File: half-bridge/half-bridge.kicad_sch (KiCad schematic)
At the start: 121 parts, among them J1 Conn_01x11_Pin, J2 MountingHole_Pad, J3 Conn_01x11_Pin, J4 Conn_01x11_Pin, J5 Conn_01x11_Pin, J6 Conn_01x11_Pin, J7 MountingHole_Pad, J8 MountingHole_Pad, J9 MountingHole_Pad, Q1 EPC2306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

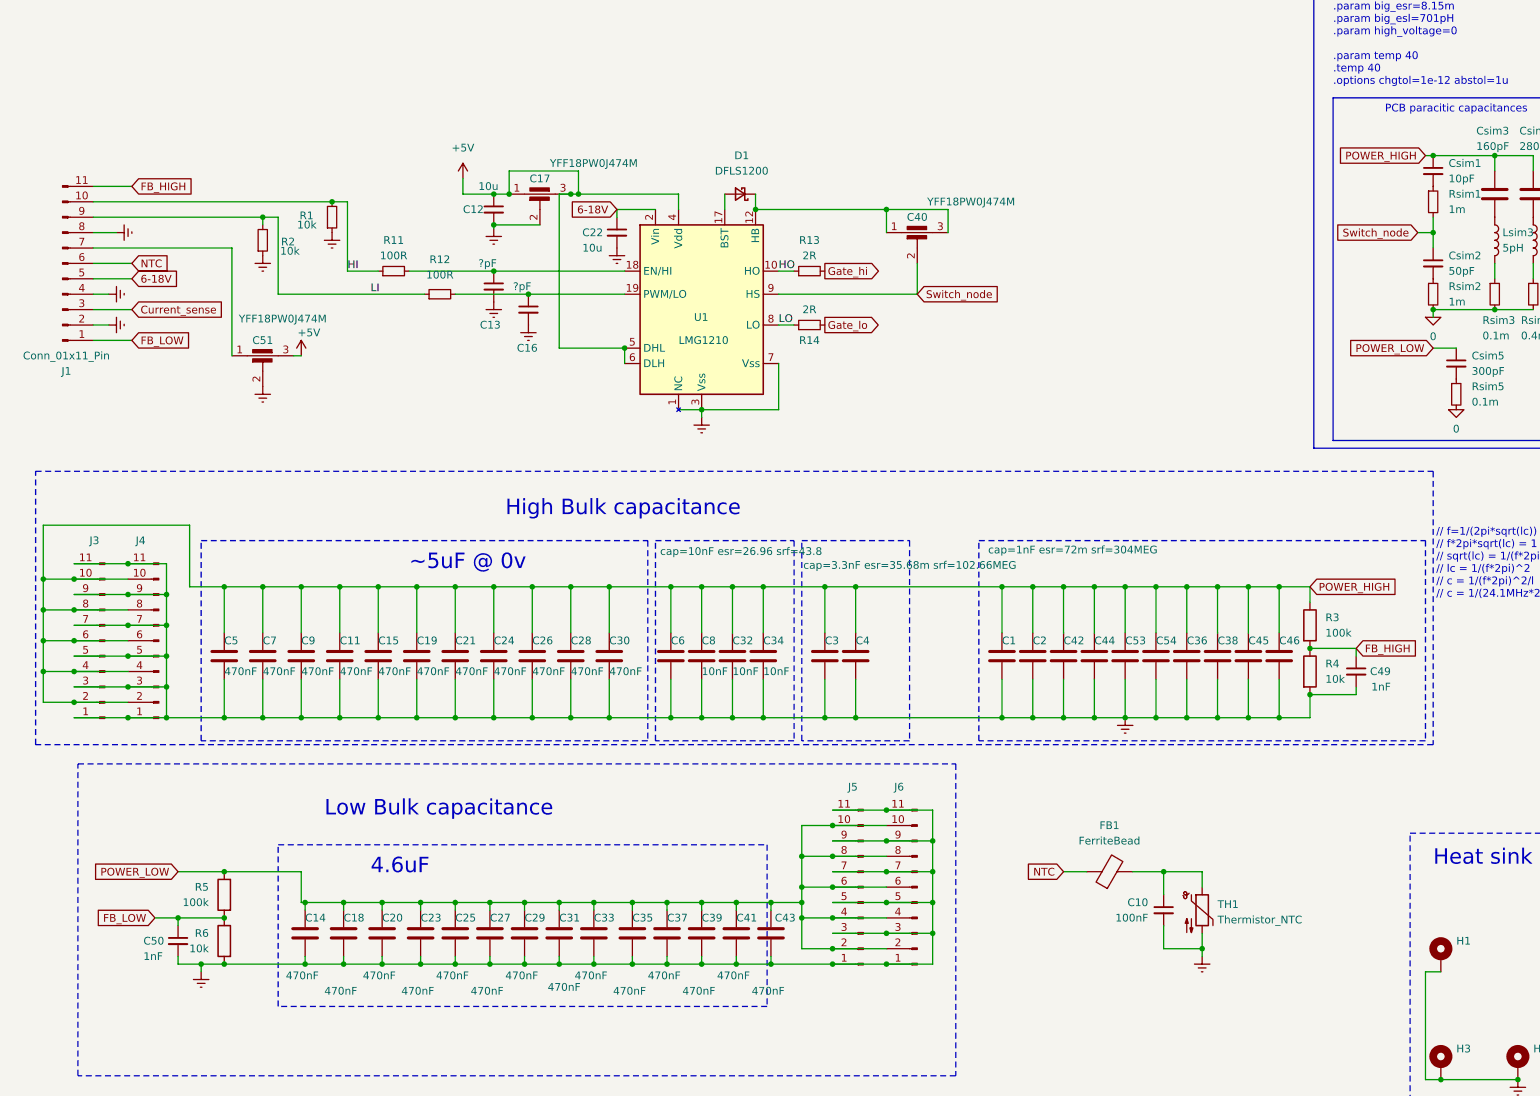
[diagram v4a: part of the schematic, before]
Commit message: Fixup reference designators, more work on controller etc
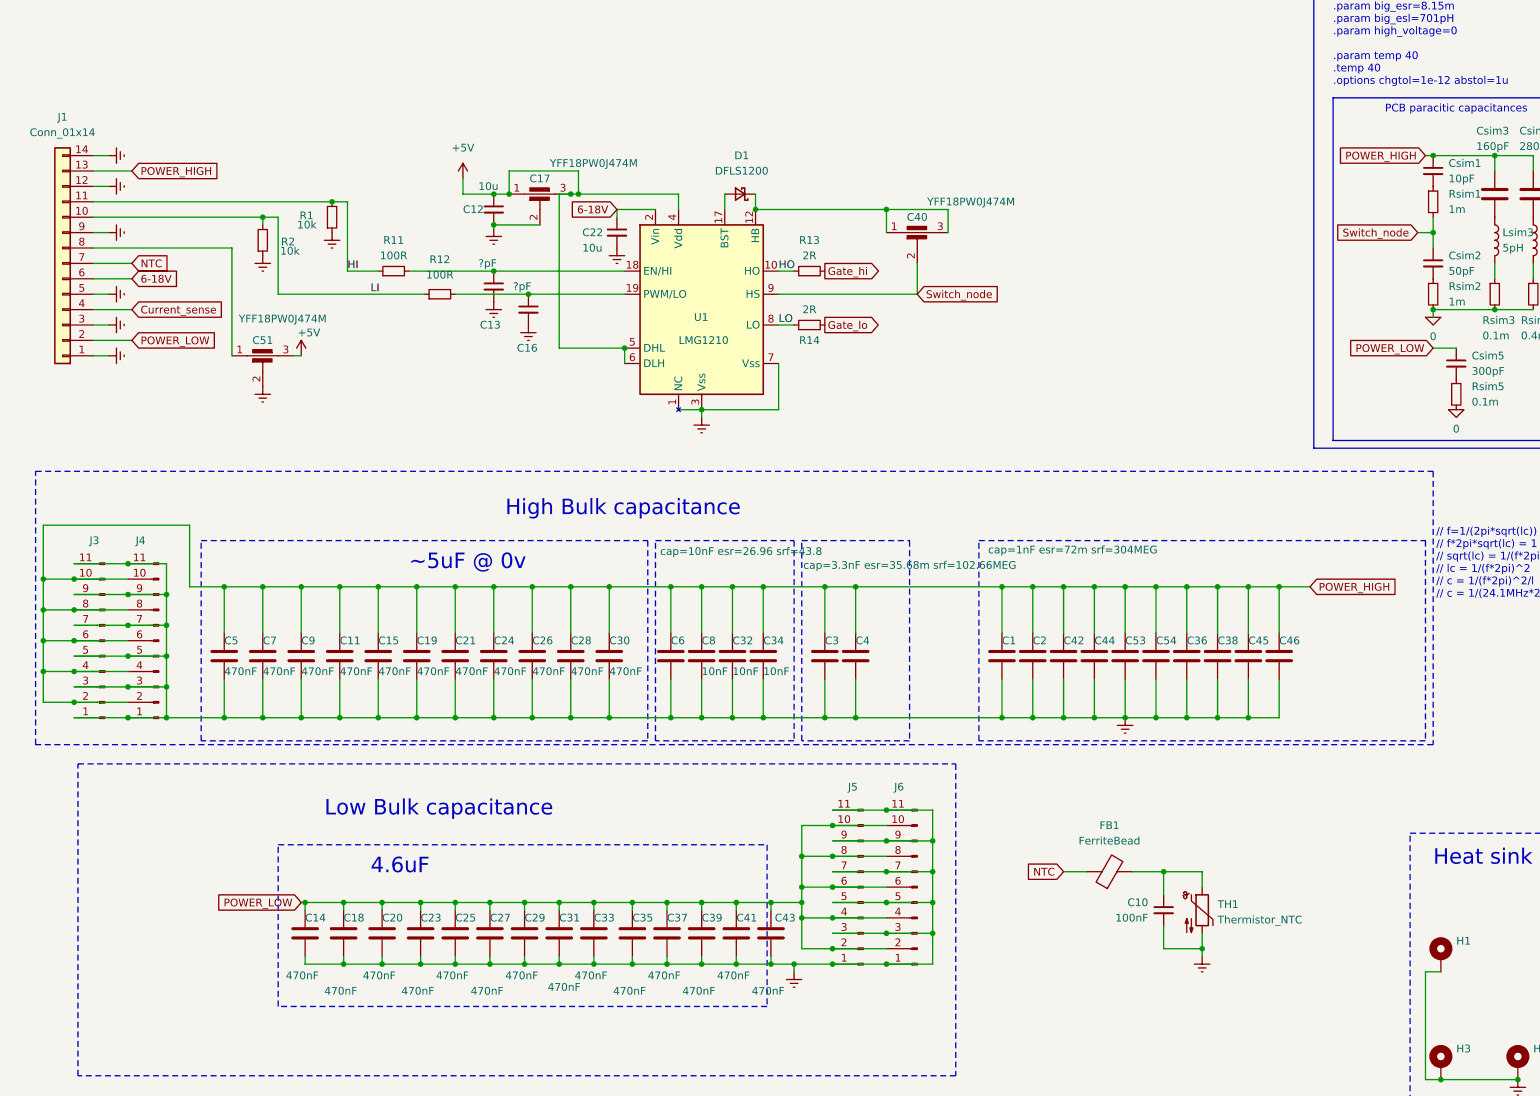
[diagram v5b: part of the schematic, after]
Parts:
- removed C49, C50: 1nF, Capacitor_SMD:C_0603_1608Metric, symbol Device:C_Small
- removed J1: Conn_01x11_Pin, Connector_PinHeader_2.54mm:PinHeader_1x11_P2.54mm_Horizontal, symbol Connector:Conn_01x11_Pin
- removed R3, R5: 100k, Resistor_SMD:R_1206_3216Metric, symbol Device:R
- removed R4, R6: 10k, Resistor_SMD:R_0805_2012Metric, symbol Device:R
- added J1: Conn_01x14, Connector_PinHeader_2.54mm:PinHeader_1x14_P2.54mm_Horizontal, symbol Connector_Generic:Conn_01x14
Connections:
- net 0: now also J1.1 (Pin_1), J1.12 (Pin_12), J1.14 (Pin_14), J1.3 (Pin_3), J1.5 (Pin_5), J1.9 (Pin_9)
- net 6-18V: now also J1.6 (Pin_6)
- net Current_sense: now also J1.4 (Pin_4)
- net HI: now also J1.11 (Pin_11)
- net LI: now also J1.10 (Pin_10)
- net NTC: now also J1.7 (Pin_7)
- net POWER_HIGH: now also J1.13 (Pin_13)
- net POWER_LOW: now also J1.2 (Pin_2)
- net at C51.1: now also J1.8 (Pin_8)

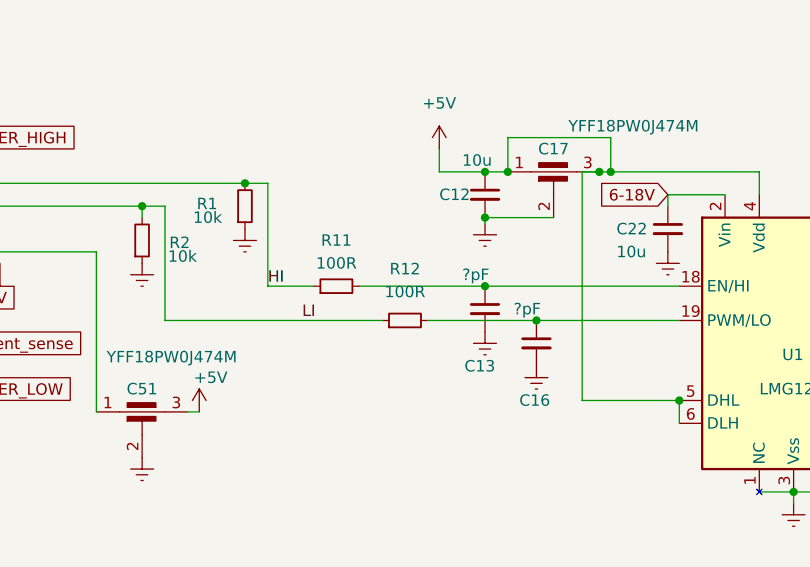
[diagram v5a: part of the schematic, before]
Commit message: WIP - Reduce size and bump to 6 layers
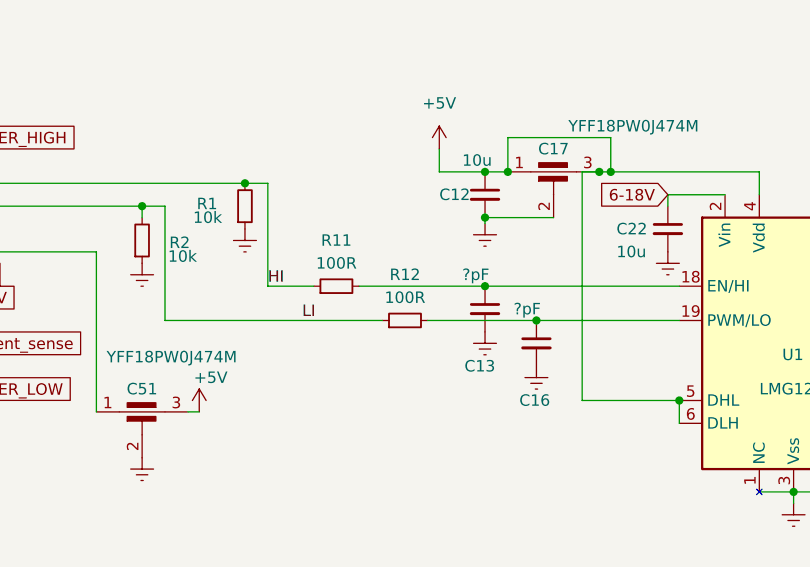
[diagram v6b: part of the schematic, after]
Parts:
- R1, R11, R12, R2: footprint Resistor_SMD:R_0603_1608Metric -> Resistor_SMD:R_0402_1005Metric
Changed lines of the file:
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@@
 			)
 		)
-		(property "Footprint" "Resistor_SMD:R_0603_1608Metric"
+		(property "Footprint" "Resistor_SMD:R_0402_1005Metric"
 			(at 73.66 90.17 0)
 			(effects
@@
 			)
 		)
-		(property "Footprint" "Resistor_SMD:R_0603_1608Metric"
+		(property "Footprint" "Resistor_SMD:R_0402_1005Metric"
 			(at 52.07 85.09 0)
 			(effects
@@
 		(fields_autoplaced yes)
 		(property "Reference" "R12"
-			(at 81.28 88.265 90)
+			(at 81.28 88.9 90)
 			(effects
 				(font
@@
 		)
 		(property "Value" "100R"
-			(at 81.28 90.805 90)
+			(at 81.28 91.44 90)
 			(effects
 				(font
@@
 			)
 		)
-		(property "Footprint" "Resistor_SMD:R_0603_1608Metric"
+		(property "Footprint" "Resistor_SMD:R_0402_1005Metric"
 			(at 81.28 93.98 0)
 			(effects
@@
 			)
 		)
-		(property "Footprint" "Resistor_SMD:R_0603_1608Metric"
+		(property "Footprint" "Resistor_SMD:R_0402_1005Metric"
 			(at 63.5 81.28 0)
 			(effects

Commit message: Cleanup, add more cap etc
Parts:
- added C49, C50, C52, C55, C56, C57: 470nF, Capacitor_SMD:C_1210_3225Metric, symbol Device:C
- added C58, C59, C60: 10uF, Capacitor_SMD:C_1210_3225Metric, symbol Device:C
- C11, C15, C19, C21, C24, C26, C28, C30, C5, C7, C9: value 470nF -> 10uF
- C38, C42, C44, C45, C46, C53, C54: footprint Capacitor_SMD:C_0402_1005Metric -> Capacitor_SMD:C_0402_1005Metric_Pad0.74x0.62mm_HandSolder
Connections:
- net 0: now also H5.1, C49.2, C50.2, C52.2, C55.2, C56.2, C57.2, C58.2, C59.2, C60.2
- net POWER_HIGH: now also C58.1, C59.1, C60.1
- net POWER_LOW: now also C49.1, C50.1, C52.1, C55.1, C56.1, C57.1; no longer H5.1
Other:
- note added: "0402 10*XnF=XnF @ 0v 10*XnF=XnF @ 48v"
- note added: "0603 2*220nF=440nF @ 0v 2*220nF=124nF @ 48v"
- note added: "0805 4*XnF=XnF @ 0v 4*XnF=XnF @ 48v"
- note added: "1210 14*10uF=140uF @ 0v 14*2.5uF=35uF @ 48v"
- note removed: "~5uF @ 0v"
- moved on the sheet: C11, C15, C19, C2, C21, C24, C26, C28, C3, C36, C38, C4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

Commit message: Update BOM
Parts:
- C11, C15, C19, C21, C24, C26, C28, C30, C5, C58, C59, C7, C9: MFR (none) -> TDK; MPN (none) -> C3225X7R2A106K250AC
- C14, C18, C20, C23, C25, C27, C29, C31, C33, C35, C37, C39, C41, C43, C49, C50, C52, C55, C56, C57: value 470nF -> 10uF; MFR (none) -> TDK; MPN (none) -> C3225X7R2A106K250AC
- C3, C4: value ${SIM.PARAMS} -> 220nF; MFR (none) -> TAIYO YUDEN; MPN (none) -> MBASH168SC7224KTCA01
- C32, C34, C8: value 10nF -> 2.2uF; MFR (none) -> TDK; MPN (none) -> C2012X7R2A225K125AC
- C51: value YFF18PW0J474M -> 470nF 6.3v; MFR (none) -> TDK; MPN (none) -> YFF18PW0J474M
- C6: value ${SIM.PARAMS} -> 2.2uF; MFR (none) -> TDK; MPN (none) -> C2012X7R2A225K125AC
- C60: MPN (none) -> C3225X7R2A106K250AC; PNR C3225X7R2A106K250AC -> (none)
- D1: MFR (none) -> Diodes Incorporated; MPN (none) -> DFLS1200
- D2, D3: MFR (none) -> Vishay; MPN (none) -> V3PM12HM3/H
- H1, H2, H3, H4, H5: MFR (none) -> Wurth; MPN (none) -> 97730256330
- L1: MFR (none) -> Coilcraft; MPN (none) -> XAL8080-222ME
- Q1, Q2: MFR (none) -> EPC; MPN (none) -> EPC2306
- R10, R7, R8, R9: MFR (none) -> Eaton; MPN (none) -> MFSA0508R0050FCM
- U2: MFR (none) -> Texas Instruments; MPN (none) -> INA293B
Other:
- note added: "0805 4*2.2uF=8.8uF @ 0v 4*453uF=1.8uF @ 48v"
- note removed: "0805 4*XnF=XnF @ 0v 4*XnF=XnF @ 48v"
